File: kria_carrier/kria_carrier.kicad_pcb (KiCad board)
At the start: 6 copper layers, 140 x 119 mm, 10 parts, among them J1 ADM6-60-01.5-L-4-2-A-TR, J2 ADM6-60-01.5-L-4-2-A-TR

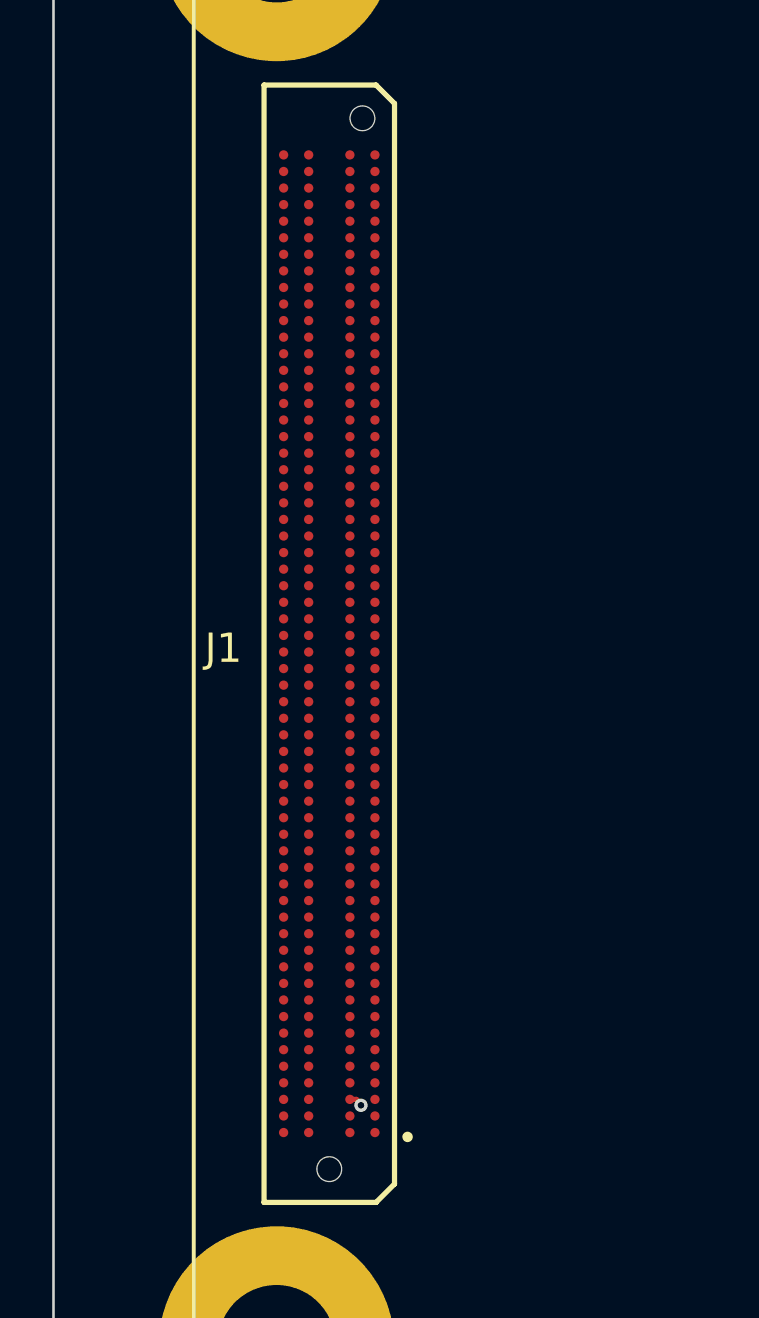
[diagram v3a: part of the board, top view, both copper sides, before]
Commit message: playing with connector fanout
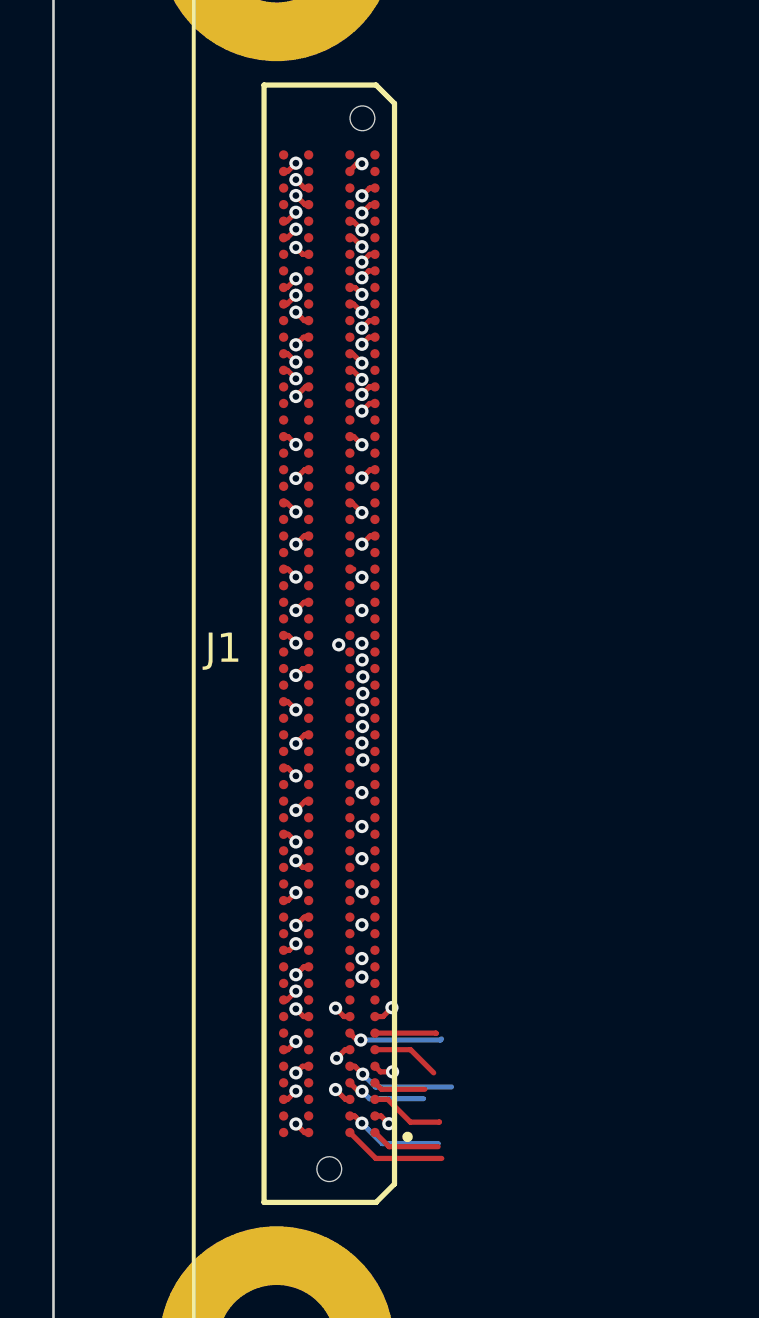
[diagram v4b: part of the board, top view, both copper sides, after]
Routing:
- net GND: track 0.55 -> 38.5 mm, vias 1 -> 75
- net unconnected-(J1-PadB05): track 0.00 -> 4.22 mm, vias 0 -> 1
- net unconnected-(J1-PadB01): track 0.00 -> 3.93 mm
- net unconnected-(J1-PadB02): track 0.00 -> 3.83 mm, vias 0 -> 1
- net unconnected-(J1-PadB07): track 0.00 -> 3.64 mm, vias 0 -> 1
- net unconnected-(J1-PadB04): track 0.00 -> 3.07 mm, vias 0 -> 1
- net unconnected-(J1-PadA03): track 0.00 -> 2.84 mm
- net unconnected-(J1-PadA01): track 0.00 -> 2.65 mm
- net unconnected-(J1-PadA06): track 0.00 -> 2.62 mm
- net unconnected-(J1-PadA07): track 0.00 -> 2.36 mm
- net unconnected-(J1-PadA04): track 0.00 -> 2.01 mm
- net unconnected-(J1-PadB30): vias 0 -> 1
- net unconnected-(J1-PadB29): vias 0 -> 1
- net unconnected-(J1-PadB28): vias 0 -> 1
- net unconnected-(J1-PadB26): vias 0 -> 1
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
